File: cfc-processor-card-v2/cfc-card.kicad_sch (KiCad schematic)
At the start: 0 parts

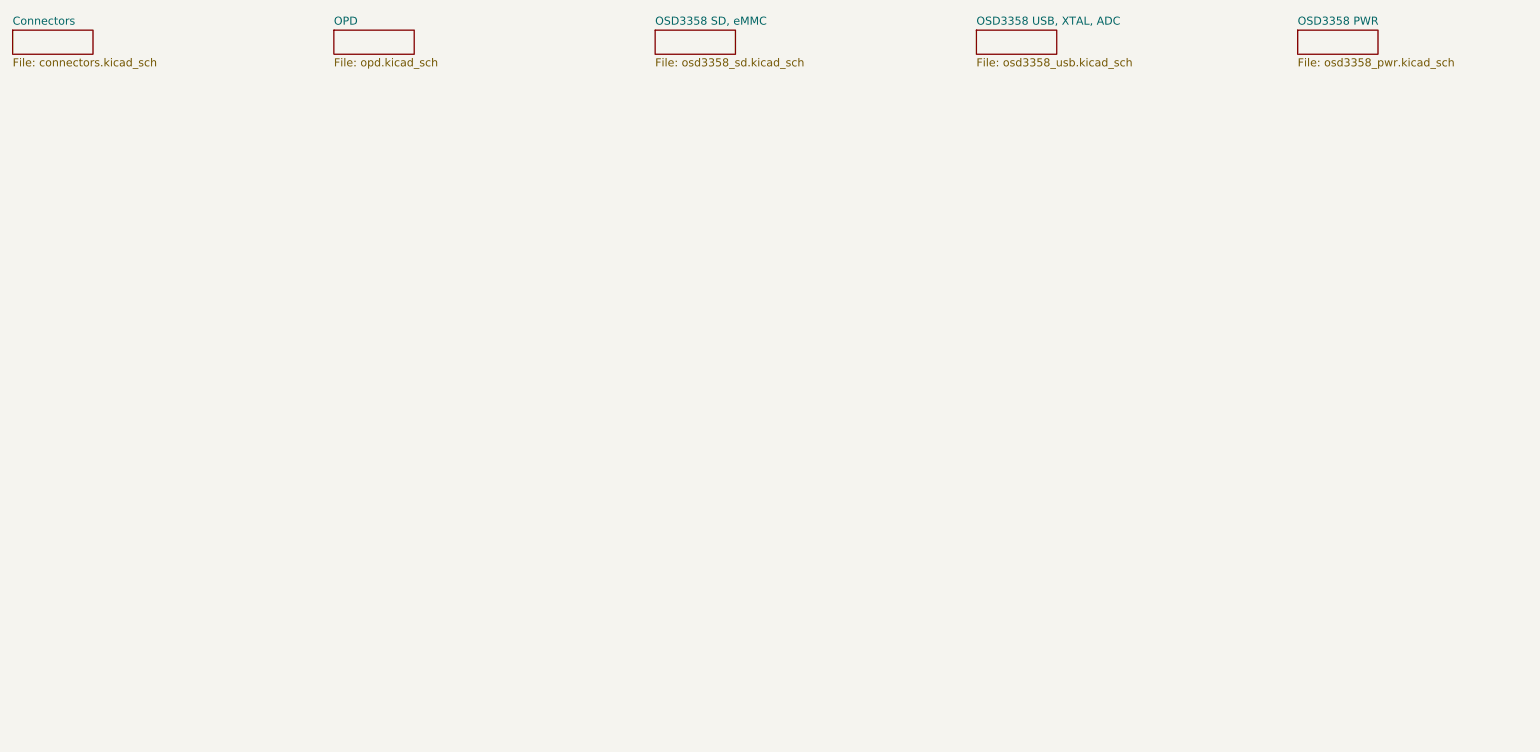
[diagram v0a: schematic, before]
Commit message: Clean up CFC Processor Card from Scott's initial import which was Gerber identical to origianl EAGLE schematic. Interestingly, this version was already changed for the v2 backplane which is great. Align schematic to be more KiCAD like based off of the C3, rename a few things, remove some outdated OPD connections, import sch into pcb, clean up pcb detritus, and import DRU settings. No longer Gerber identicial, but it's now ready for further polishing for fabrication.
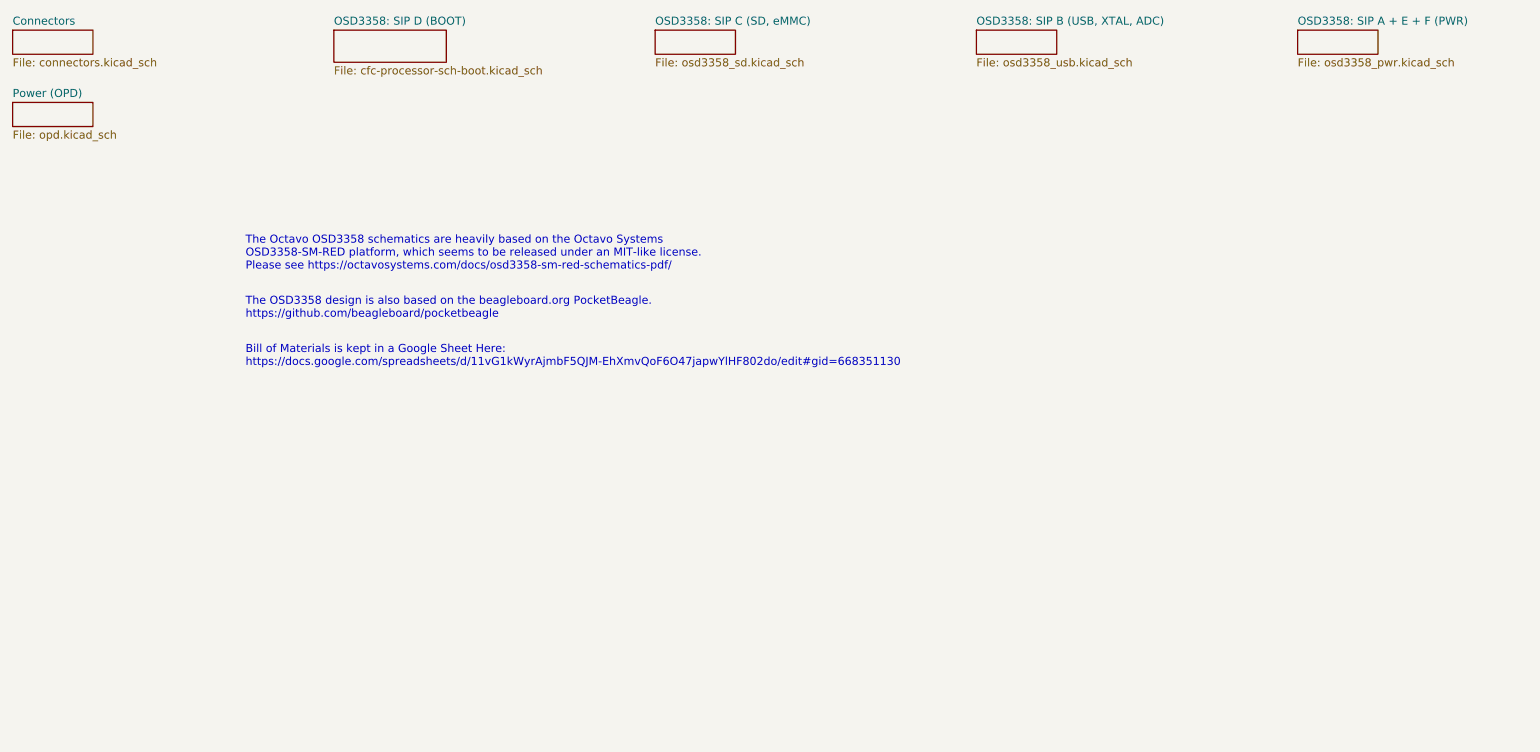
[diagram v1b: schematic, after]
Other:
- sheet OPD renamed Power (OPD)
- sheet OSD3358 PWR renamed OSD3358: SIP A + E + F (PWR)
- sheet OSD3358 SD, eMMC renamed OSD3358: SIP C (SD, eMMC)
- sheet OSD3358 USB, XTAL, ADC renamed OSD3358: SIP B (USB, XTAL, ADC)
- added sheet OSD3358: SIP D (BOOT) (cfc-processor-sch-boot.kicad_sch)
- note added: "Bill of Materials is kept in a Google Sheet Here: https://docs.google.com/spreadsheets/d/11vG1kWyrAjmbF5QJM-EhXmvQoF6O47japwYlHF802do/edit#gid=668351130"
- note added: "The OSD3358 design is also based on the beagleboard.org PocketBeagle. https://github.com/beagleboard/pocketbeagle"
- note added: "The Octavo OSD3358 schematics are heavily based on the Octavo Systems OSD3358-SM-RED platform, which seems to be released under an MIT-like license. Please see https://octavosystems.com/docs/osd3358-sm-red-schematics-pdf/"
- company: (none) -> Portland State Aerospace Society
- title: (none) -> OreSat CFC Processor Card

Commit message: Final polish on schematic and PCB. Cleaned up BOM, fixed github issues which were not really issues. Lots of BOM cleanup, with MPNs and DPNs.
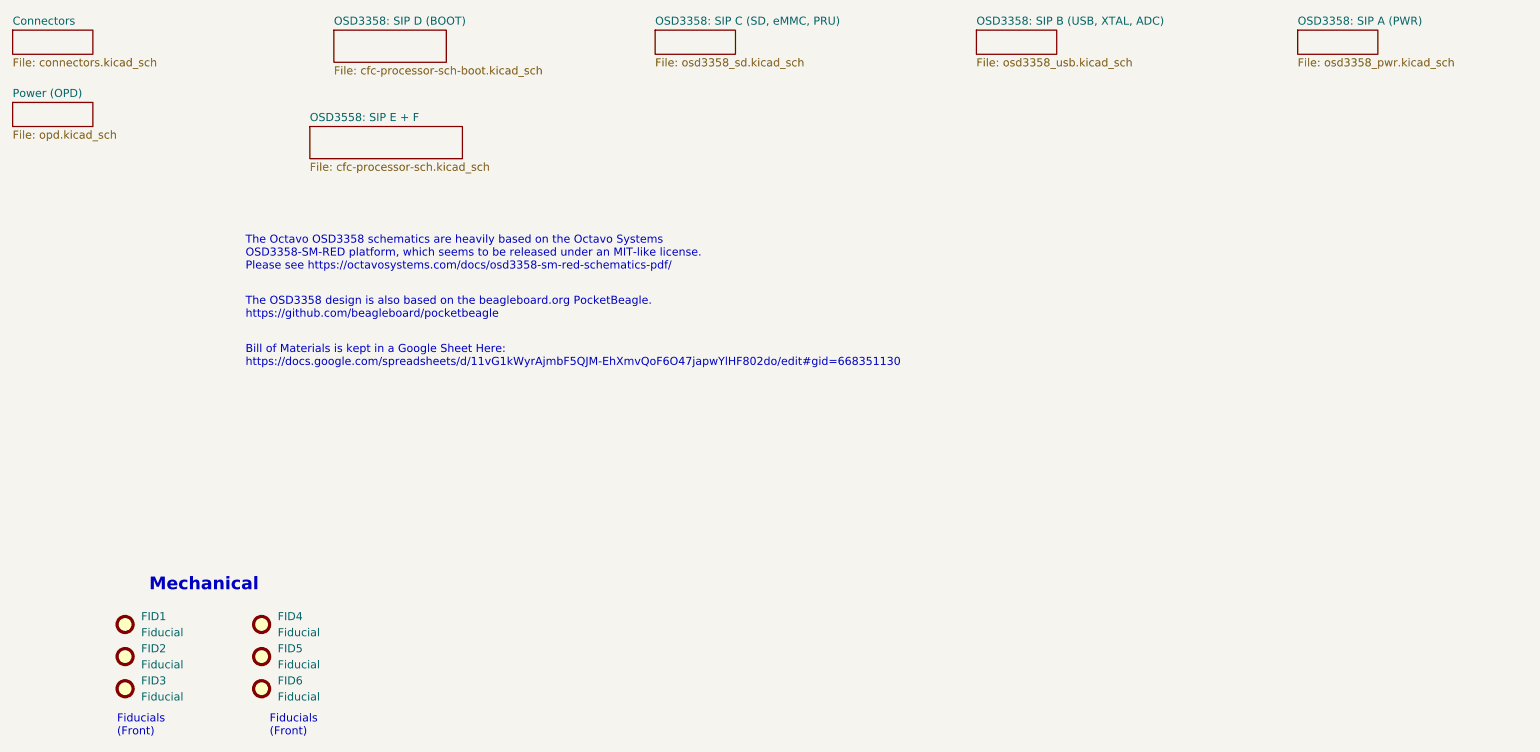
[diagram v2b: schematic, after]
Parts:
- added FID1, FID2, FID3, FID4, FID5, FID6: Fiducial, Fiducial:Fiducial_1mm_Mask2mm, symbol Mechanical:Fiducial
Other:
- sheet OSD3358: SIP A + E + F (PWR) renamed OSD3358: SIP A (PWR)
- sheet OSD3358: SIP C (SD, eMMC) renamed OSD3358: SIP C (SD, eMMC, PRU)
- added sheet OSD3558: SIP E + F (cfc-processor-sch.kicad_sch)
- note added: "Fiducials (Front)"
- note added: "Mechanical"
